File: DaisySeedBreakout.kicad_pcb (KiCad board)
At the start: 2 copper layers, 151 parts, among them J2 5027740891, J2 Conn_02x08, J4 5027740891, J5 Conn_02x08, J6 Conn_02x08, U1 NE5532, U1 TCA6424ARGJR, U2 NE5532, U3 MAX9814, U5 MAX9814

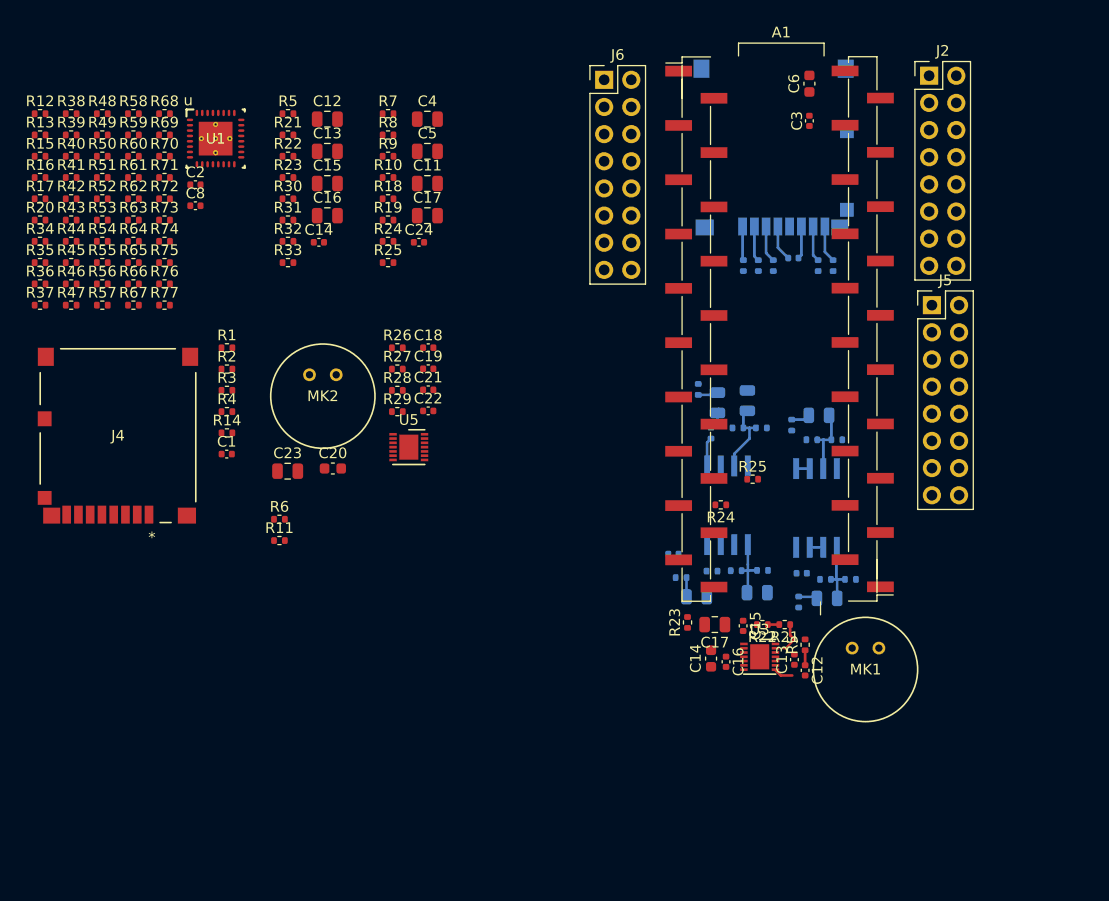
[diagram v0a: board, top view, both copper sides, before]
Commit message: Fixed ultralibrarian library with capital letter difference
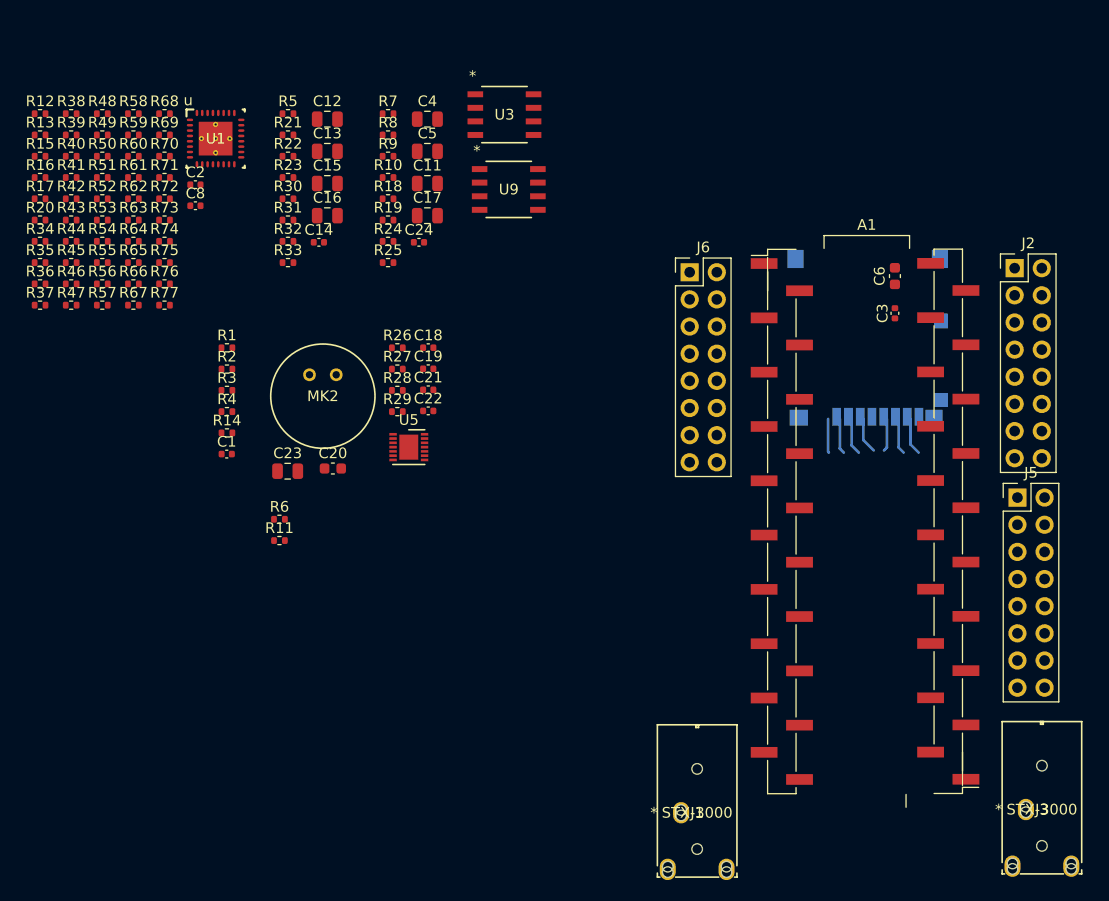
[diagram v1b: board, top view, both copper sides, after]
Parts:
- removed the C1 at (130.5, 68.4)
- removed C10, C7: 0.1uF, Capacitor_SMD:C_0402_1005Metric
- removed the C11 at (136.3, 51.8)
- removed the C12 at (135.0, 75.7)
- removed the C13 at (134.0, 74.7)
- removed the C14 at (126.2, 74.6)
- removed the C15 at (129.2, 71.5)
- removed the C16 at (127.6, 74.9)
- removed the C17 at (126.5, 71.4)
- removed the C2 at (129.6, 50.5)
- removed the C4 at (137.0, 68.9)
- removed the C5 at (122.7, 64.8)
- removed the C8 at (126.8, 50.6)
- removed C9: 10U, Capacitor_SMD:C_0805_2012Metric
- removed the J2 at (132.0, 26.8)
- removed MK1: Microphone_Condenser, microphone:MIC_AOM-6545_PUI
- removed the R1 at (130.9, 53.0)
- removed the R10 at (133.8, 52.7)
- removed the R11 at (130.6, 37.8)
- removed the R12 at (132.0, 37.8)
- removed the R13 at (136.2, 37.8)
- removed the R14 at (131.0, 66.3)
- removed the R15 at (126.3, 66.4)
- removed the R16 at (125.0, 49.4)
- removed the R17 at (123.4, 67.0)
- removed the R18 at (139.2, 67.2)
- removed the R19 at (136.9, 67.2)
- removed the R2 at (128.7, 53.0)
- removed the R20 at (137.6, 37.8)
- removed the R21 at (133.1, 71.4)
- removed the R22 at (131.0, 71.4)
- removed the R23 at (124.0, 71.2)
- removed the R24 at (127.1, 60.2)
- removed the R25 at (130.1, 57.8)
- removed the R3 at (128.6, 66.4)
- removed the R4 at (126.2, 53.5)
- removed the R5 at (135.0, 73.3)
- removed the R6 at (129.2, 37.8)
- removed the R7 at (135.6, 54.1)
- removed the R8 at (138.0, 54.1)
- removed the R9 at (134.4, 69.3)
- removed the U1 at (127.7, 60.2)
- removed U2: NE5532, N5532_2:PS8-M
- added J1: STX-3000, Ultralibrarian:STX-3000_KYC, F.Cu at (123.4, 89.0)
- added J3: STX-3000, Ultralibrarian:STX-3000_KYC, F.Cu at (155.6, 88.7)
- added U9: ~, Ultralibrarian:D8_TEX, F.Cu at (107.3, 30.7)
- J4: moved to B.Cu
- U3: value MAX9814 -> ~; footprint Package_DFN_QFN:DFN-14-1EP_3x3mm_P0.4mm_EP1.78x2.35mm -> Ultralibrarian:D8_TEX
- moved J4 70.7 mm to (140.8, 44.6), turned to 180 degrees
- moved U3 56.1 mm to (106.9, 23.7)
- moved A1 19.7 mm to (133.1, 37.6)
- moved J2 19.7 mm to (154.6, 38.1)
- moved C3 19.7 mm to (143.4, 42.3)
- moved J5 19.7 mm to (154.9, 59.5)
- moved C6 19.7 mm to (143.4, 38.8)
- moved J6 19.7 mm to (124.2, 38.4)
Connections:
- U3 pad 1: Net-(U3-CT) -> Net-(U3A--A)
- U3 pad 2: +5V_ISO -> Net-(U3A--A)
- U3 pad 3: Net-(U3-CG) -> Net-(U3A-+IN_A)
- U3 pad 5: +5V_ISO -> Net-(U3B-+IN_B)
- U3 pad 6: Net-(U3-MICOUT) -> Net-(U3B--B)
- U3 pad 7: GND -> Net-(U3B--B)
- U3 pad 8: Net-(U3-MICIN) -> +5V_ISO
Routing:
- net Net-(U1A-+): track 7.08 -> 0.00 mm
- net Net-(U2A-+): track 6.87 -> 0.00 mm
- net Net-(U2B-+): track 6.17 -> 0.00 mm
- net Net-(U1B-+): track 5.98 -> 0.00 mm
- net SD_D1: track 3.47 -> 0.00 mm
- net /microSD/D0: track 0.00 -> 3.47 mm
- net SD_CMD: track 3.43 -> 0.00 mm
- net /microSD/D3: track 0.00 -> 3.43 mm
- net /microSD/CMD: track 0.00 -> 3.35 mm
- net +3.3V: track 3.35 -> 0.00 mm
- net SD_D0: track 3.34 -> 0.00 mm
- net SD_D3: track 3.30 -> 0.00 mm
- net /microSD/D2: track 0.00 -> 3.30 mm
- net SD_D2: track 3.18 -> 0.00 mm
- net (no net): track 0.00 -> 3.18 mm
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
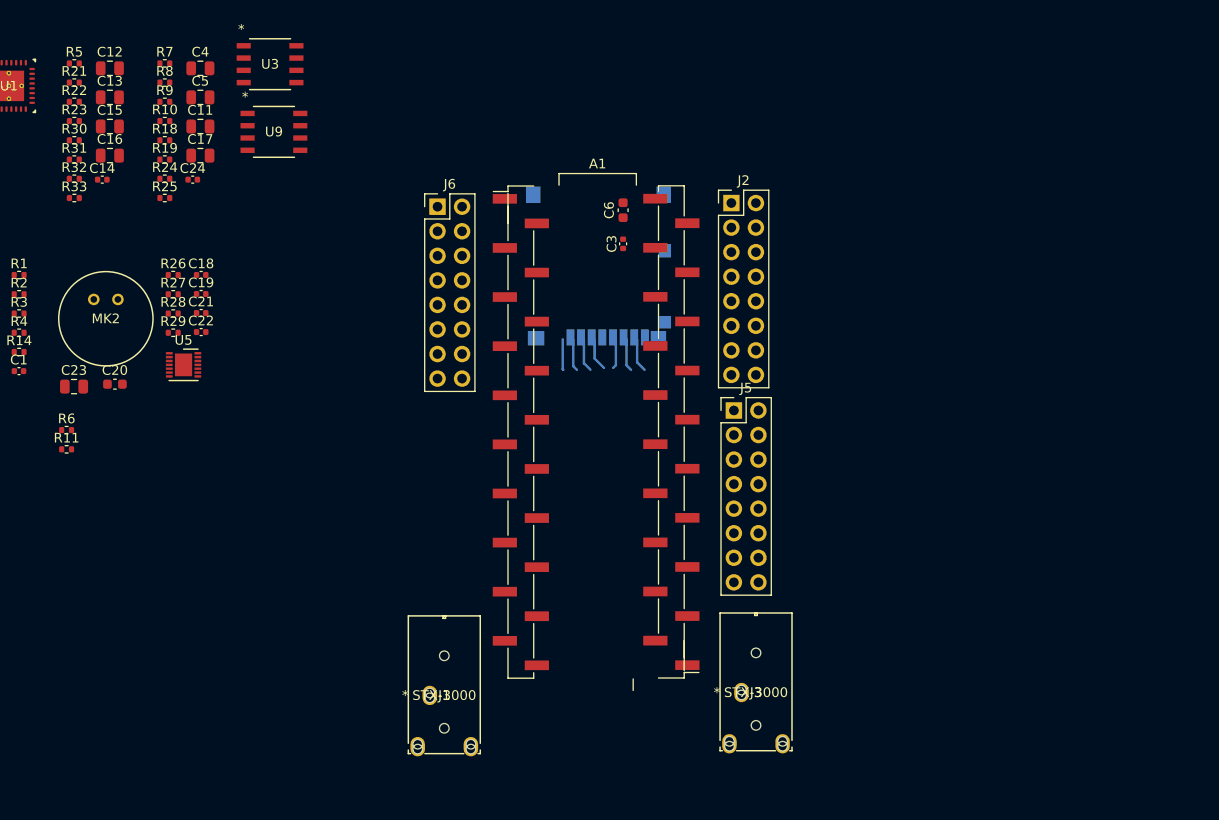
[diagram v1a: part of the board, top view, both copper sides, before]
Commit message: added knob headers, MIDI in header
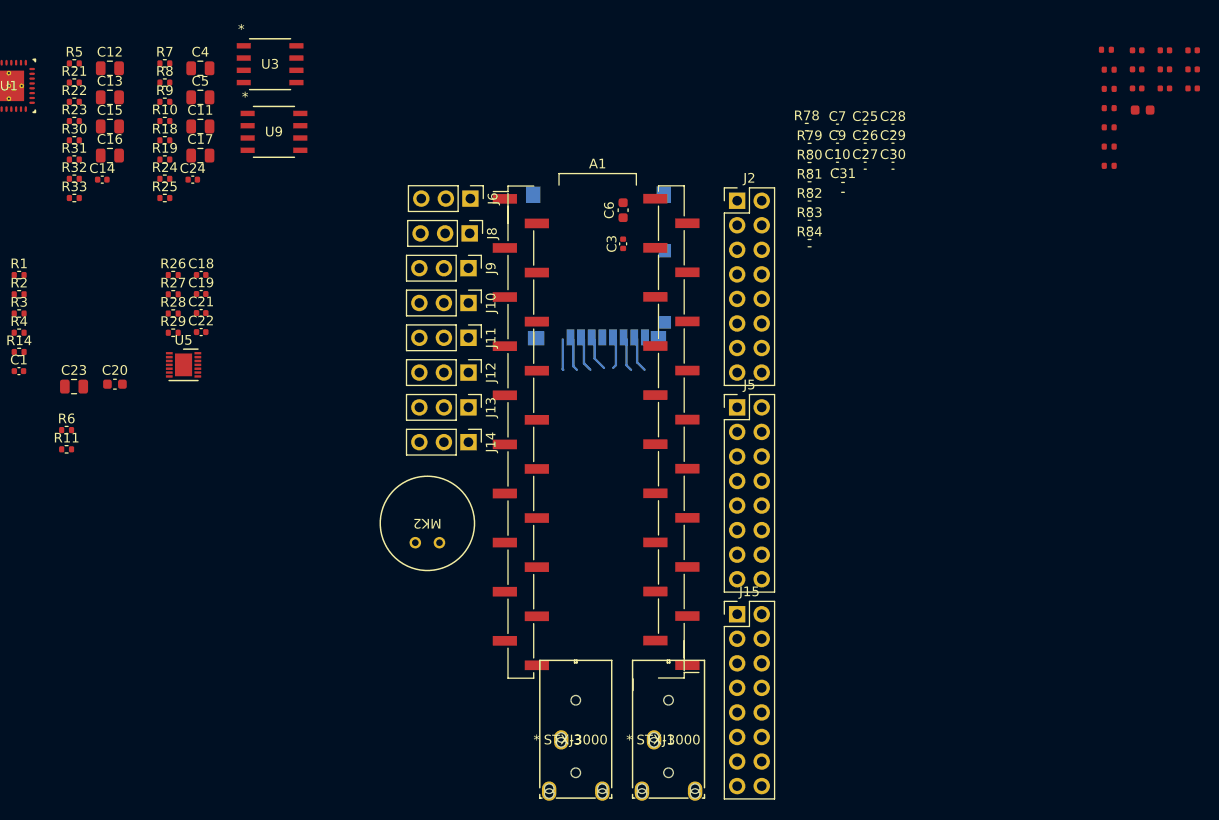
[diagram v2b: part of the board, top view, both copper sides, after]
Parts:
- added C10: 0.1uF, Capacitor_SMD:C_0402_1005Metric, F.Cu at (165.6, 34.2)
- added C25: 0.1uF, Capacitor_SMD:C_0402_1005Metric, F.Cu at (168.4, 30.3)
- added C26: 0.1uF, Capacitor_SMD:C_0402_1005Metric, F.Cu at (168.4, 32.2)
- added C27: 0.1uF, Capacitor_SMD:C_0402_1005Metric, F.Cu at (168.4, 34.2)
- added C28: 0.1uF, Capacitor_SMD:C_0402_1005Metric, F.Cu at (171.3, 30.3)
- added C29: 0.1uF, Capacitor_SMD:C_0402_1005Metric, F.Cu at (171.3, 32.2)
- added C30: 0.1uF, Capacitor_SMD:C_0402_1005Metric, F.Cu at (171.3, 34.2)
- added C31: 0.1uF, Capacitor_SMD:C_0603_1608Metric, F.Cu at (166.2, 36.4)
- added C7: 0.1uF, Capacitor_SMD:C_0402_1005Metric, F.Cu at (165.6, 30.3)
- added C9: 0.1uF, Capacitor_SMD:C_0402_1005Metric, F.Cu at (165.6, 32.2)
- added J10: Conn_01x03, Connector_PinHeader_2.54mm:PinHeader_1x03_P2.54mm_Vertical, F.Cu at (127.4, 48.4)
- added J11: Conn_01x03, Connector_PinHeader_2.54mm:PinHeader_1x03_P2.54mm_Vertical, F.Cu at (127.4, 52.0)
- added J12: Conn_01x03, Connector_PinHeader_2.54mm:PinHeader_1x03_P2.54mm_Vertical, F.Cu at (127.4, 55.6)
- added J13: Conn_01x03, Connector_PinHeader_2.54mm:PinHeader_1x03_P2.54mm_Vertical, F.Cu at (127.4, 59.2)
- added J14: Conn_01x03, Connector_PinHeader_2.54mm:PinHeader_1x03_P2.54mm_Vertical, F.Cu at (127.4, 62.8)
- added J15: Conn_02x08, Connector_PinHeader_2.54mm:PinHeader_2x08_P2.54mm_Vertical, F.Cu at (155.2, 80.6)
- added J8: Conn_01x03, Connector_PinHeader_2.54mm:PinHeader_1x03_P2.54mm_Vertical, F.Cu at (127.5, 41.2)
- added J9: Conn_01x03, Connector_PinHeader_2.54mm:PinHeader_1x03_P2.54mm_Vertical, F.Cu at (127.4, 44.8)
- added R78: 1k, Resistor_SMD:R_0402_1005Metric, F.Cu at (162.4, 30.2)
- added R79: 1k, Resistor_SMD:R_0402_1005Metric, F.Cu at (162.7, 32.3)
- added R80: 1k, Resistor_SMD:R_0402_1005Metric, F.Cu at (162.7, 34.2)
- added R81: 1k, Resistor_SMD:R_0402_1005Metric, F.Cu at (162.7, 36.2)
- added R82: 1k, Resistor_SMD:R_0402_1005Metric, F.Cu at (162.7, 38.2)
- added R83: 1k, Resistor_SMD:R_0402_1005Metric, F.Cu at (162.7, 40.2)
- added R84: 1k, Resistor_SMD:R_0402_1005Metric, F.Cu at (162.7, 42.2)
- J6: value Conn_02x08 -> Conn_01x03; footprint Connector_PinHeader_2.54mm:PinHeader_2x08_P2.54mm_Vertical -> Connector_PinHeader_2.54mm:PinHeader_1x03_P2.54mm_Vertical
- moved MK2 39.4 mm to (123.2, 71.2), turned to 180 degrees
- moved J1 23.7 mm to (146.6, 93.6)
- moved J3 19.3 mm to (137.0, 93.6)
- moved J6 3.50 mm to (127.6, 37.6), turned to -90 degrees
- moved J2 0.65 mm to (155.2, 37.8)
- moved J5 0.47 mm to (155.2, 59.2)
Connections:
- A1 pad 14: unconnected-(A1-USART1_TX-Pad14) -> /MIDI_UART_TX
- A1 pad 15: unconnected-(A1-USART1_RX-Pad15) -> /MIDI_UART_RX
- A1 pad 22: unconnected-(A1-ADC_0-Pad22) -> /AI0
- A1 pad 23: unconnected-(A1-ADC_1-Pad23) -> /AI1
- A1 pad 24: unconnected-(A1-ADC_2-Pad24) -> /AI2
- A1 pad 25: unconnected-(A1-ADC_3-Pad25) -> /AI3
- A1 pad 26: unconnected-(A1-ADC_4-Pad26) -> /AI4
- A1 pad 27: unconnected-(A1-ADC_5-Pad27) -> /AI5
- A1 pad 28: unconnected-(A1-ADC_6-Pad28) -> /AI6
- J2 pad 1: /I2C 24 GPIO/A0 -> /I2C 24 GPIO/B0
- J2 pad 11: /I2C 24 GPIO/A5 -> /I2C 24 GPIO/B5
- J2 pad 13: /I2C 24 GPIO/A6 -> /I2C 24 GPIO/B6
- J2 pad 15: /I2C 24 GPIO/A7 -> /I2C 24 GPIO/B7
- J2 pad 3: /I2C 24 GPIO/A1 -> /I2C 24 GPIO/B1
- J2 pad 5: /I2C 24 GPIO/A2 -> /I2C 24 GPIO/B2
- J2 pad 7: /I2C 24 GPIO/A3 -> /I2C 24 GPIO/B3
- J2 pad 9: /I2C 24 GPIO/A4 -> /I2C 24 GPIO/B4
- J5 pad 1: /I2C 24 GPIO/B0 -> /I2C 24 GPIO/C0
- J5 pad 11: /I2C 24 GPIO/B5 -> /I2C 24 GPIO/C5
- J5 pad 13: /I2C 24 GPIO/B6 -> /I2C 24 GPIO/C6
- J5 pad 15: /I2C 24 GPIO/B7 -> /I2C 24 GPIO/C7
- J5 pad 3: /I2C 24 GPIO/B1 -> /I2C 24 GPIO/C1
- J5 pad 5: /I2C 24 GPIO/B2 -> /I2C 24 GPIO/C2
- J5 pad 7: /I2C 24 GPIO/B3 -> /I2C 24 GPIO/C3
- J5 pad 9: /I2C 24 GPIO/B4 -> /I2C 24 GPIO/C4
- J6 pad 1: /I2C 24 GPIO/C0 -> GND
- J6 pad 2: GND -> +9V
- J6 pad 3: /I2C 24 GPIO/C1 -> /Audio Out/AUDIO_OUT_L_EXT

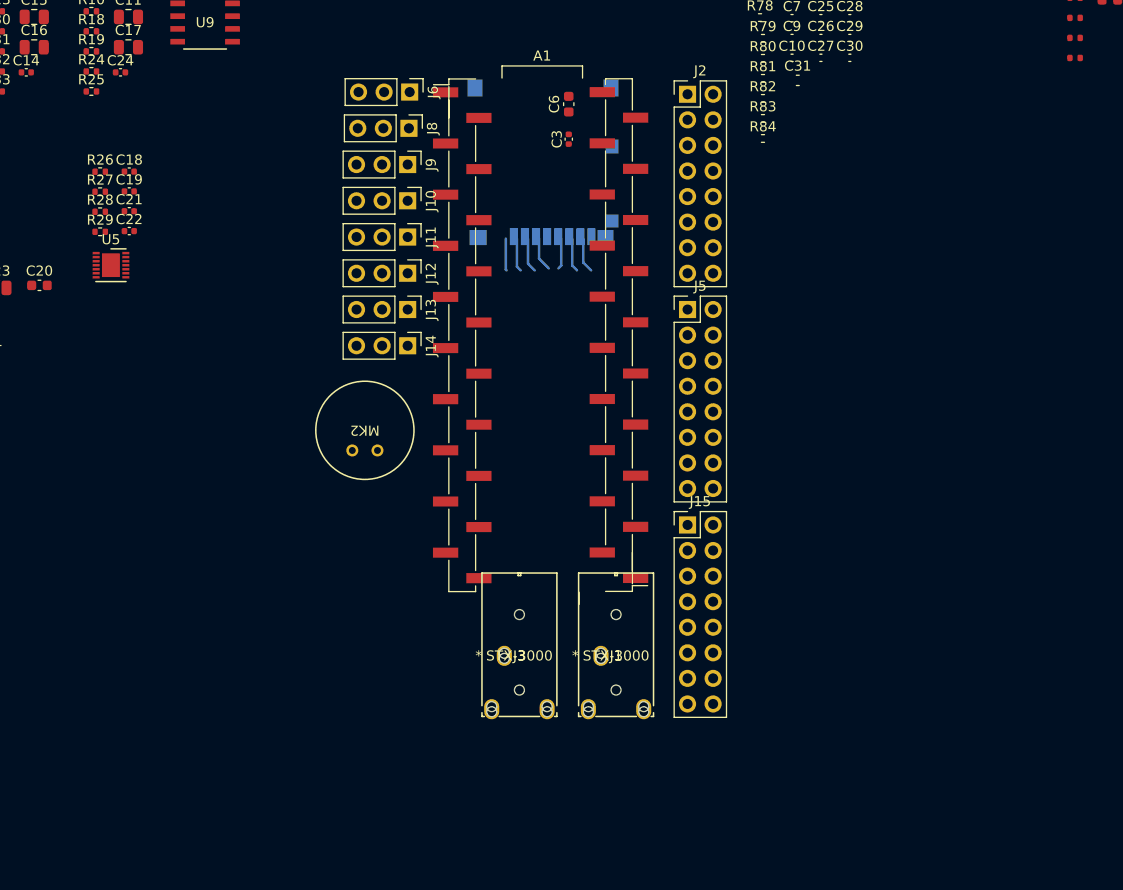
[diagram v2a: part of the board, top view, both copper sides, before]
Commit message: added double high audio jack
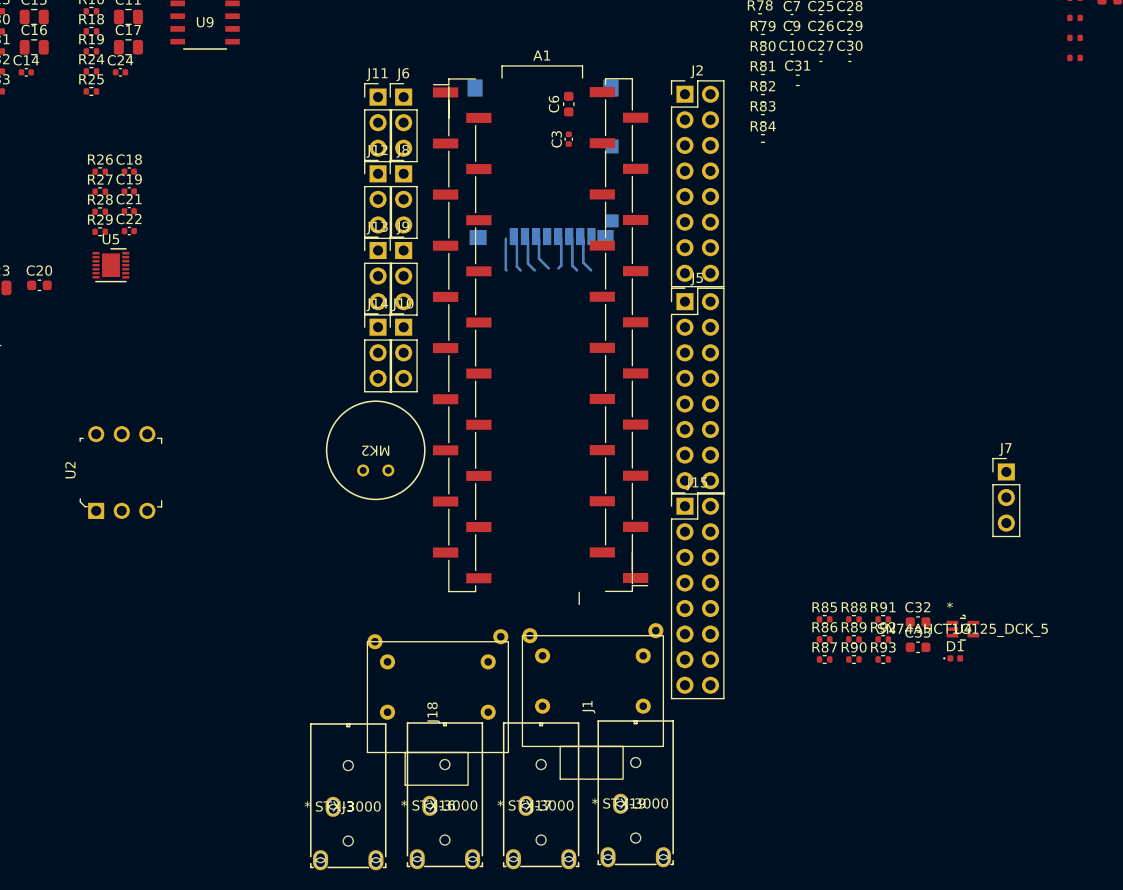
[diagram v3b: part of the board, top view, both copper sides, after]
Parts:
- added C32: 0.1uF, Capacitor_SMD:C_0603_1608Metric, F.Cu at (178.1, 90.2)
- added C33: 0.1uF, Capacitor_SMD:C_0603_1608Metric, F.Cu at (178.1, 92.8)
- added D1: D_Schottky, Diode_SMD:D_0402_1005Metric, F.Cu at (181.8, 93.9)
- added J16: STX-3000, Ultralibrarian:STX-3000_KYC, F.Cu at (129.6, 108.5)
- added J17: STX-3000, Ultralibrarian:STX-3000_KYC, F.Cu at (139.2, 108.5)
- added J18: ~, Ultralibrarian:STX-4235-3-3-N, F.Cu at (130.4, 99.2)
- added J19: STX-3000, Ultralibrarian:STX-3000_KYC, F.Cu at (148.5, 108.3)
- added J7: Conn_01x03, Connector_PinHeader_2.54mm:PinHeader_1x03_P2.54mm_Vertical, F.Cu at (186.9, 75.3)
- added R85: 220, Resistor_SMD:R_0402_1005Metric, F.Cu at (168.8, 90.0)
- added R86: SPARE, Resistor_SMD:R_0402_1005Metric, F.Cu at (168.8, 92.0)
- added R87: SPARE, Resistor_SMD:R_0402_1005Metric, F.Cu at (168.8, 94.0)
- added R88: 0, Resistor_SMD:R_0402_1005Metric, F.Cu at (171.7, 90.0)
- added R89: 270, Resistor_SMD:R_0402_1005Metric, F.Cu at (171.7, 92.0)
- added R90: 220, Resistor_SMD:R_0402_1005Metric, F.Cu at (171.7, 94.0)
- added R91: SPARE, Resistor_SMD:R_0402_1005Metric, F.Cu at (174.6, 90.0)
- added R92: 220, Resistor_SMD:R_0402_1005Metric, F.Cu at (174.6, 92.0)
- added R93: SPARE, Resistor_SMD:R_0402_1005Metric, F.Cu at (174.6, 94.0)
- added U2: H11L1M, digikey-footprints:DIP-6_W7.62mm, F.Cu at (96.5, 79.2)
- added U4: SN74AHCT1G125_DCK_5, Ultralibrarian:DCK5, F.Cu at (182.6, 91.0)
- J1: value STX-3000 -> ~; footprint Ultralibrarian:STX-3000_KYC -> Ultralibrarian:STX-4235-3-3-N
- moved J3 22.7 mm to (120.0, 108.6)
- moved J11 14.2 mm to (124.5, 38.1), turned to 0 degrees
- moved J10 12.6 mm to (127.0, 61.0), turned to 0 degrees
- moved J12 10.3 mm to (124.5, 45.7), turned to 0 degrees
- moved J9 8.55 mm to (127.0, 53.3), turned to 0 degrees
- moved J13 6.56 mm to (124.5, 53.3), turned to 0 degrees
- moved J1 5.06 mm to (145.8, 98.6), turned to 90 degrees
- moved J8 4.55 mm to (127.0, 45.7), turned to 0 degrees
- moved J14 3.47 mm to (124.5, 61.0), turned to 0 degrees
- moved MK2 2.26 mm to (124.2, 73.2)
- moved J15 1.88 mm to (154.9, 78.7)
- moved J5 0.82 mm to (154.9, 58.4)
- moved J6 0.78 mm to (127.0, 38.1), turned to 0 degrees
- moved J2 0.26 mm to (154.9, 37.8)
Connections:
- J3 pad 1: GND -> unconnected-(J3-Pad1)
- J3 pad 2: /Audio Out/AUDIO_OUT_R_EXT -> unconnected-(J3-Pad2)
- J3 pad 3: /Audio Out/AUDIO_OUT_L_EXT -> unconnected-(J3-Pad3)

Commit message: adding 3d models
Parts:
- moved C31 152.2 mm to (34.0, 112.1)
- moved R81 152.2 mm to (30.6, 111.9)
- moved R82 152.2 mm to (30.6, 113.9)
- moved R83 152.2 mm to (30.6, 115.9)
- moved R84 152.2 mm to (30.6, 117.9)
- moved C1 106.6 mm to (186.9, 67.4)
- moved C14 106.6 mm to (195.5, 47.5)
- moved R10 106.6 mm to (201.9, 41.5)
- moved R18 106.6 mm to (201.9, 43.5)
- moved R19 106.6 mm to (201.9, 45.5)
- moved R24 106.6 mm to (201.9, 47.5)
- moved R25 106.6 mm to (201.9, 49.4)
- moved R7 106.6 mm to (201.9, 35.5)
- moved R8 106.6 mm to (201.9, 37.5)
- moved R9 106.6 mm to (201.9, 39.5)
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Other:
- board outline added: 41.1 x 66 mm
